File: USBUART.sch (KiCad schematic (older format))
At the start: 7 parts, among them U501 CH340G, Y501 12MHz

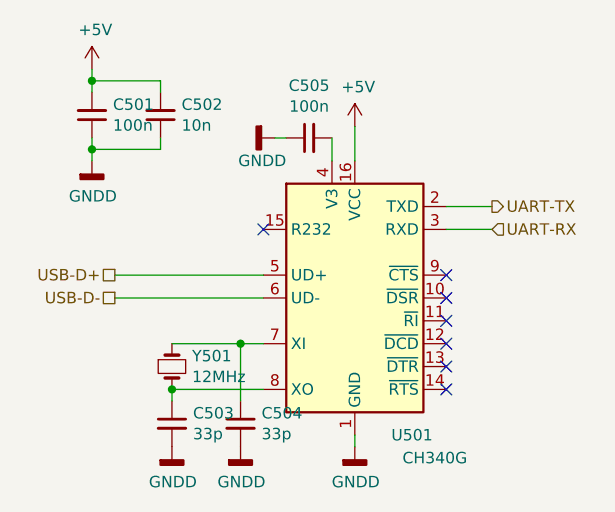
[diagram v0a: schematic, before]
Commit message: PCB layout 90% finished
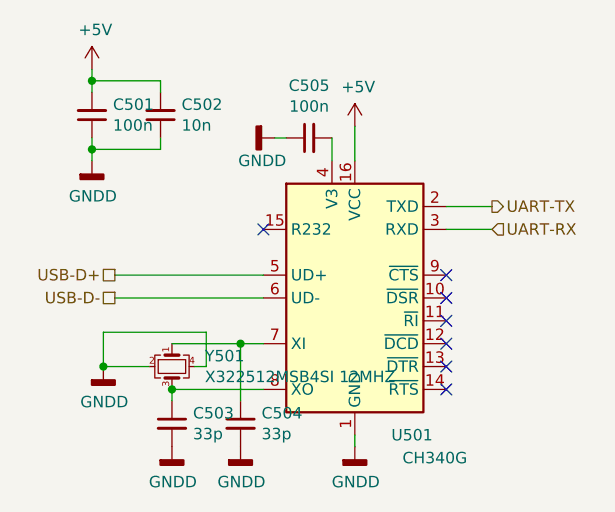
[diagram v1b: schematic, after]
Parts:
- removed Y501: 12MHz, Crystal:Crystal_SMD_0603-2Pin_6.0x3.5mm, symbol Device:Crystal_Small
- added Y501: X322512MSB4SI 12MHZ, Crystal:Crystal_SMD_3225-4Pin_3.2x2.5mm, symbol Device:Crystal_GND24_Small
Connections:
- net GNDD: now also Y501.2, Y501.4
- net at C504.1, U501.7 (XI): now also Y501.1
- net at C503.1, U501.8 (XO): now also Y501.3
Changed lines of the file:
@@
 P 2900 1800
 AR Path="/604CDA98" Ref="#PWR?"  Part="1"
-AR Path="/604C325D/604CDA98" Ref="#PWR0506"  Part="1"
-F 0 "#PWR0506" H 2900 1650 50  0001 C CNN
+AR Path="/604C325D/604CDA98" Ref="#PWR0507"  Part="1"
+F 0 "#PWR0507" H 2900 1650 50  0001 C CNN
 F 1 "+5V" H 2915 1973 50  0000 C CNN
 F 2 "" H 2900 1800 50  0001 C CNN
@@
 P 2550 1850
 AR Path="/604CDAC6" Ref="#PWR?"  Part="1"
-AR Path="/604C325D/604CDAC6" Ref="#PWR0505"  Part="1"
-F 0 "#PWR0505" H 2550 1600 50  0001 C CNN
+AR Path="/604C325D/604CDAC6" Ref="#PWR0506"  Part="1"
+F 0 "#PWR0506" H 2550 1600 50  0001 C CNN
 F 1 "GNDD" V 2650 1900 50  0000 R CNN
 F 2 "" H 2550 1850 50  0001 C CNN
@@
 NoConn ~ 3300 2550
 NoConn ~ 3300 2450
-$Comp
-L Device:Crystal_Small Y?
-U 1 1 604CDAD5
-P 2100 2850
-AR Path="/604CDAD5" Ref="Y?"  Part="1"
-AR Path="/604C325D/604CDAD5" Ref="Y501"  Part="1"
-F 0 "Y501" V 2054 2938 50  0000 L CNN
-F 1 "12MHz" V 2145 2938 50  0000 L CNN
-F 2 "Crystal:Crystal_SMD_0603-2Pin_6.0x3.5mm" H 2100 2850 50  0001 C CNN
-F 3 "~" H 2100 2850 50  0001 C CNN
-	1    2100 2850
-	0    1    1    0
-$EndComp
 $Comp
 L Device:C_Small C?
@@
 Wire Wire Line
 	2100 3000 2100 2950
-Connection ~ 2100 2950
 Wire Wire Line
 	2400 3000 2400 2750
@@
 P 2100 3200
 AR Path="/604CDAEE" Ref="#PWR?"  Part="1"
-AR Path="/604C325D/604CDAEE" Ref="#PWR0503"  Part="1"
-F 0 "#PWR0503" H 2100 2950 50  0001 C CNN
+AR Path="/604C325D/604CDAEE" Ref="#PWR0504"  Part="1"
+F 0 "#PWR0504" H 2100 2950 50  0001 C CNN
 F 1 "GNDD" H 2104 3045 50  0000 C CNN
 F 2 "" H 2100 3200 50  0001 C CNN
@@
 P 2400 3200
 AR Path="/604CDAF4" Ref="#PWR?"  Part="1"
-AR Path="/604C325D/604CDAF4" Ref="#PWR0504"  Part="1"
-F 0 "#PWR0504" H 2400 2950 50  0001 C CNN
+AR Path="/604C325D/604CDAF4" Ref="#PWR0505"  Part="1"
+F 0 "#PWR0505" H 2400 2950 50  0001 C CNN
 F 1 "GNDD" H 2404 3045 50  0000 C CNN
 F 2 "" H 2400 3200 50  0001 C CNN
@@
 P 2900 3200
 AR Path="/604CDAFA" Ref="#PWR?"  Part="1"
-AR Path="/604C325D/604CDAFA" Ref="#PWR0507"  Part="1"
-F 0 "#PWR0507" H 2900 2950 50  0001 C CNN
+AR Path="/604C325D/604CDAFA" Ref="#PWR0508"  Part="1"
+F 0 "#PWR0508" H 2900 2950 50  0001 C CNN
 F 1 "GNDD" H 2904 3045 50  0000 C CNN
 F 2 "" H 2900 3200 50  0001 C CNN
@@
 Wire Wire Line
 	2900 3150 2900 3200
+$Comp
+L Device:Crystal_GND24_Small Y501
+U 1 1 5F04CC98
+P 2100 2850
+F 0 "Y501" V 2054 2994 50  0000 L CNN
+F 1 "X322512MSB4SI 12MHZ" V 2145 2994 50  0000 L CNN
+F 2 "Crystal:Crystal_SMD_3225-4Pin_3.2x2.5mm" H 2100 2850 50  0001 C CNN
+F 3 "~" H 2100 2850 50  0001 C CNN
+	1    2100 2850
+	0    1    1    0
+$EndComp
+Connection ~ 2100 2950
+$Comp
+L power:GNDD #PWR?
+U 1 1 5F04D960
+P 1800 2850
+AR Path="/5F04D960" Ref="#PWR?"  Part="1"
+AR Path="/604C325D/5F04D960" Ref="#PWR0503"  Part="1"
+F 0 "#PWR0503" H 1800 2600 50  0001 C CNN
+F 1 "GNDD" H 1804 2695 50  0000 C CNN
+F 2 "" H 1800 2850 50  0001 C CNN
+F 3 "" H 1800 2850 50  0001 C CNN
+	1    1800 2850
+	1    0    0    -1
+$EndComp
+Wire Wire Line
+	2000 2850 1800 2850
+Wire Wire Line
+	2200 2850 2250 2850
+Wire Wire Line
+	2250 2850 2250 2700
+Wire Wire Line
+	2250 2700 1800 2700
+Wire Wire Line
+	1800 2700 1800 2850
+Connection ~ 1800 2850
 $EndSCHEMATC
